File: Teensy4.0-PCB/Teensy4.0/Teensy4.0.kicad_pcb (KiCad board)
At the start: 4 copper layers, 76 x 58 mm, 74 parts, among them IC2 NC7WZ241K8X, J1 24-27, J2 28-31, U1 Teensy4.0, U2 NRF24, U3 TXS0104ERGYR, U4 TPS62143RGTT, U5 MIC5504-1.8YM5, U6 ICM-20948, U7 TXS0104ERGYR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

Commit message: changed some stuff
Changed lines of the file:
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@@
 			(pintype "passive")
 		)
-		(model "/home/jirakornsukmee/Documents/Morphing-Robot/Teensy4.0-PCB/models/IND_SRP2512_BRN.step"
+		(model "/Users/jirakornsukmee/Documents/Morphing-Robot/Teensy4.0-PCB/models/IND_SRP2512_BRN.step"
 			(offset
 				(xyz 0 0 0)
@@
 			(font
 				(size 1 1)
-				(thickness 0.25)
-				(bold yes)
+				(thickness 0.15)
 			)
 			(justify left bottom)
@@
 			(font
 				(size 1 1)
-				(thickness 0.25)
-				(bold yes)
+				(thickness 0.15)
 			)
 			(justify left bottom)
@@
 			(font
 				(size 1 1)
-				(thickness 0.25)
-				(bold yes)
+				(thickness 0.15)
 			)
 			(justify left bottom)
@@
 			(font
 				(size 1 1)
-				(thickness 0.25)
-				(bold yes)
+				(thickness 0.15)
 			)
 			(justify left bottom)
@@
 			(font
 				(size 1 1)
-				(thickness 0.25)
-				(bold yes)
+				(thickness 0.15)
 			)
 			(justify left bottom)
@@
 			(font
 				(size 1 1)
-				(thickness 0.25)
-				(bold yes)
+				(thickness 0.15)
 			)
 			(justify left bottom)
@@
 			(font
 				(size 1 1)
-				(thickness 0.25)
-				(bold yes)
+				(thickness 0.15)
 			)
 			(justify left bottom)
@@
 			(font
 				(size 1 1)
-				(thickness 0.25)
-				(bold yes)
+				(thickness 0.15)
 			)
 			(justify left bottom)
@@
 	)
 	(zone
-		(net 0)
-		(net_name "")
-		(layer "F.Cu")
-		(hatch edge 0.5)
-		(connect_pads
-			(clearance 0)
-		)
-		(min_thickness 0.25)
-		(filled_areas_thickness no)
-		(keepout
-			(tracks allowed)
-			(vias allowed)
-			(pads allowed)
-			(copperpour not_allowed)
-			(footprints allowed)
-		)
-		(fill
-			(thermal_gap 0.5)
-			(thermal_bridge_width 0.5)
-		)
-		(polygon
-			(pts
-				(xy 149.748 104.7) (xy 149.748 102.1) (xy 152.548 102.1) (xy 152.548 104.7)
-			)
-		)
-	)
-	(zone
 		(net 5)
 		(net_name "GND")
@@
 			)
 		)
+	)
+	(zone
+		(net 0)
+		(net_name "")
+		(layers "F.Cu" "In1.Cu" "In2.Cu" "B.Cu")
+		(hatch edge 0.5)
+		(connect_pads
+			(clearance 0)
+		)
+		(min_thickness 0.25)
+		(filled_areas_thickness no)
+		(keepout
+			(tracks allowed)
+			(vias allowed)
+			(pads allowed)
+			(copperpour not_allowed)
+			(footprints allowed)
+		)
+		(fill
+			(thermal_gap 0.5)
+			(thermal_bridge_width 0.5)
+		)
+		(polygon
+			(pts
+				(xy 149.748 104.7) (xy 149.748 102.1) (xy 152.548 102.1) (xy 152.548 104.7)
+			)
+		)

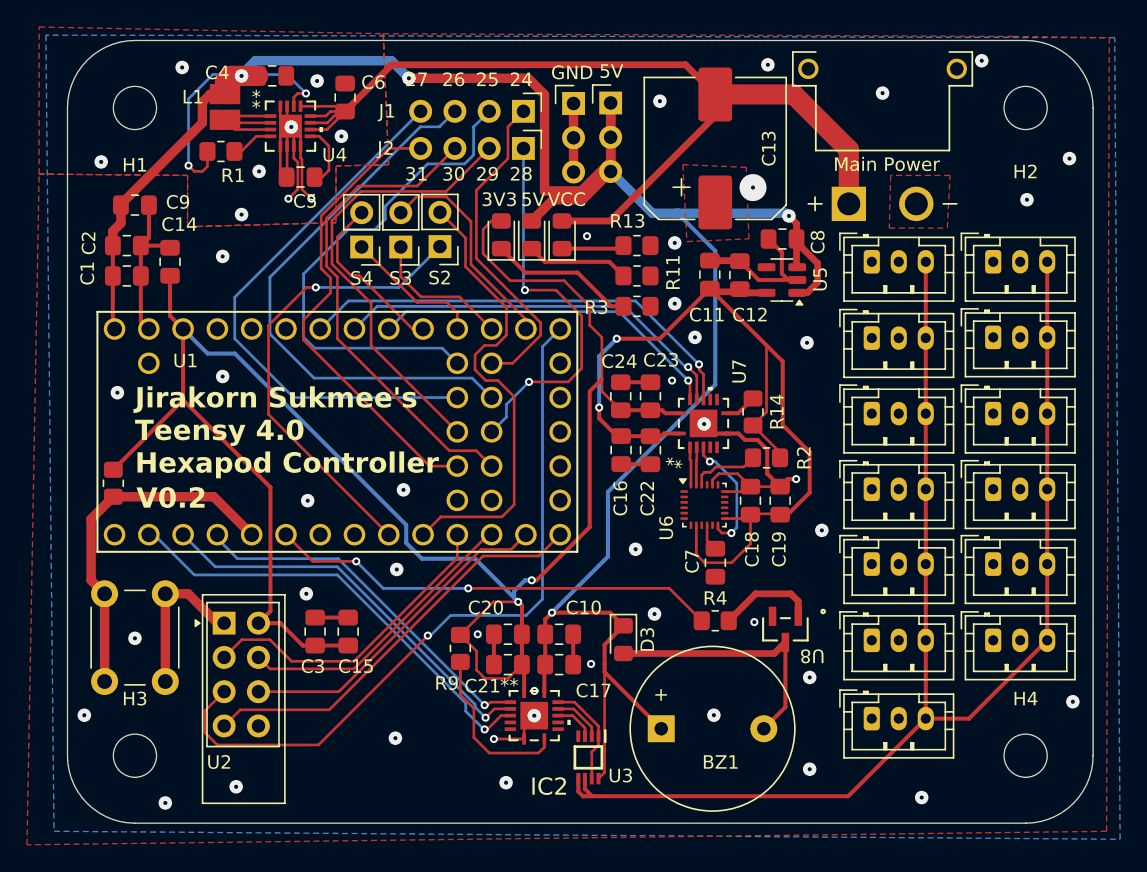
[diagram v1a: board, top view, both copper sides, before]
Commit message: updated pcb: changed from nrf24l01 to lora ra-02
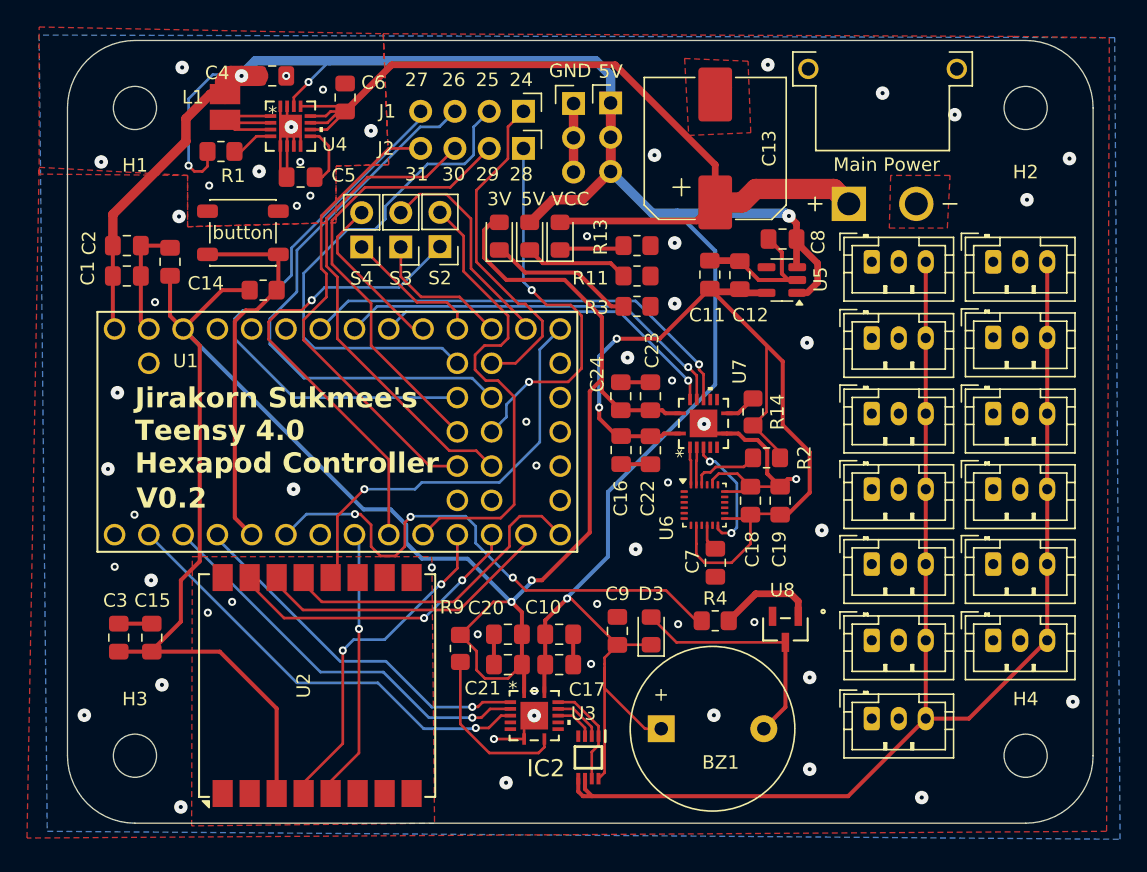
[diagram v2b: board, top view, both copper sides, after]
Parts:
- removed 3V3: 3V3 | Red, Diode_SMD:D_0805_2012Metric_Pad1.15x1.40mm_HandSolder
- removed button1: SW_Push, Button_Switch_THT:SW_PUSH_6mm
- added 3V: 3V3 | Red, Diode_SMD:D_0805_2012Metric_Pad1.15x1.40mm_HandSolder, F.Cu at (136.0, 83.5)
- added button: SW_Push, Button_Switch_SMD:SW_SPST_PTS647_Sx38, F.Cu at (117.0, 83.2)
- U2: value NRF24 -> Ai-Thinker-Ra-02; footprint RF_Module:nRF24L01_Breakout -> RF_Module:Ai-Thinker-Ra-01-LoRa
- moved C9 47.7 mm to (144.8, 112.8), turned to 90 degrees
- moved R7 18.1 mm to (118.5, 87.5), turned to 180 degrees
- moved C15 14.6 mm to (110.2, 113.2)
- moved C3 14.6 mm to (107.8, 113.2)
- moved U2 8.30 mm to (122.5, 116.8), turned to 90 degrees
- moved D3 2.15 mm to (147.2, 112.8), turned to 90 degrees
- moved 5V 0.18 mm to (138.2, 83.5)
- moved VCC 0.18 mm to (140.5, 83.5)
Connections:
- C13 pad 1: GND -> VCC
- C13 pad 2: VCC -> GND
- U1 pad 11: /NRF_CE -> /LORA_CE
- U1 pad 12: /NRF_CSN -> /LORA_CSN
- U1 pad 13: /NRF_MOSI -> /LORA_MOSI
- U1 pad 14: /NRF_MISO -> /LORA_MISO
- U1 pad 20: /NRF_SCK -> /LORA_SCK
- U1 pad 8: unconnected-(U1-6_OUT1D-Pad8) -> /LORA_IRQ
- U2 pad 2: +3V3 -> GND
- U2 pad 3: /NRF_CE -> +3V3
- U2 pad 4: /NRF_CSN -> /LORA_CE
- U2 pad 5: /NRF_SCK -> /LORA_IRQ
- U2 pad 6: /NRF_MOSI -> unconnected-(U2-DIO1-Pad6)
- U2 pad 7: /NRF_MISO -> unconnected-(U2-DIO2-Pad7)
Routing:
- net /NRF_SCK: track 54.0 -> 0.00 mm, vias 1 -> 0
- net /LORA_SCK: track 0.00 -> 31.2 mm, vias 0 -> 1
- net /NRF_MISO: track 30.8 -> 0.00 mm
- net /LORA_CE: track 0.00 -> 25.5 mm, vias 0 -> 2
- net /NRF_MOSI: track 24.6 -> 0.00 mm
- net /LORA_MISO: track 0.00 -> 23.9 mm
- net /NRF_CE: track 23.4 -> 0.00 mm
- net /LORA_CSN: track 0.00 -> 22.5 mm, vias 0 -> 2
- net /LORA_MOSI: track 0.00 -> 22.2 mm
- net /NRF_CSN: track 21.8 -> 0.00 mm
- net GND: track 95.7 -> 74.9 mm, vias 51 -> 58
- net /LORA_IRQ: track 0.00 -> 20.4 mm, vias 0 -> 1
- net +3V3: track 142.4 -> 154.5 mm
- net +5V: track 187.8 -> 179.4 mm, vias 6 -> 5
- net /buzzer: track 33.5 -> 40.0 mm, vias 2 -> 3
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
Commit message: updates
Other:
- board text added: "Jirakorn Sukmee's"
- board text added: "Teensy 4.0 Hexapod Controller"
- board text added: "and Tapa._.nont"
- board text removed: "Jirakorn Sukmee's Teensy 4.0 Hexapod Controller"
